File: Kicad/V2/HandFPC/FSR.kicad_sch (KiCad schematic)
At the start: 1 part

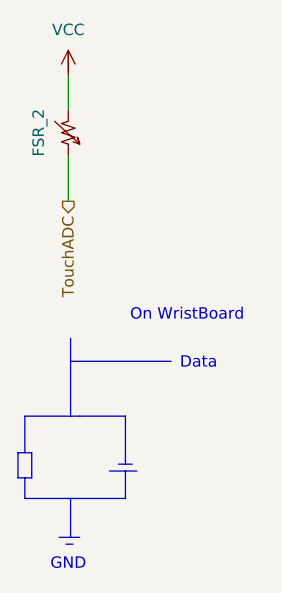
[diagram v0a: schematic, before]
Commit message: hand FPC pass erc no warning no error
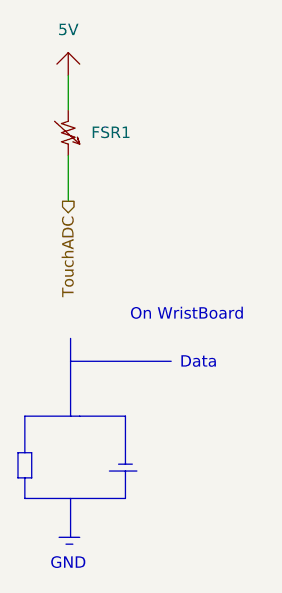
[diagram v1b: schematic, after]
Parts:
- removed FSR_2: (no value), MyGlove:PinHeader_1x02_P2.54mm_Vertical, symbol G-Love:FSR
- added FSR1: (no value), symbol G-Love-Symbols:FSR
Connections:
- net TouchADC: now also FSR1.1
- new net 5V: FSR1.2
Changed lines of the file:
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@@
 	)
 	(symbol
-		(lib_id "G-Love:VCC")
-		(at 33.02 24.13 0)
+		(lib_id "G-Love-Symbols:+5V")
+		(at 33.02 22.86 0)
 		(unit 1)
 		(body_style 1)
@@
 		(dnp no)
 		(fields_autoplaced yes)
-		(property "Reference" "#PWR017"
-			(at 36.83 25.908 0)
+		(property "Reference" "#PWR01"
+			(at 35.56 22.2249 0)
 			(hide yes)
 			(show_name no)
@@
 					(size 1.27 1.27)
 				)
+				(justify left)
 			)
 		)
-		(property "Value" "VCC"
+		(property "Value" "5V"
 			(at 33.02 20.32 0)
 			(show_name no)
@@
 		)
 		(property "Footprint" ""
-			(at 33.02 24.13 0)
+			(at 33.02 22.86 0)
 			(hide yes)
 			(show_name no)
@@
 		)
 		(property "Datasheet" ""
-			(at 33.02 24.13 0)
+			(at 33.02 22.86 0)
 			(hide yes)
 			(show_name no)
@@
 		)
 		(property "Description" ""
-			(at 33.02 24.13 0)
+			(at 33.02 22.86 0)
 			(hide yes)
 			(show_name no)
@@
 			(project "HandFPC"
 				(path "/7221f3d8-f3bc-4a50-a6fd-69c2d8ca27db/03ec02f7-0970-4f94-9fde-cabfa1326b5e"
-					(reference "#PWR017")
+					(reference "#PWR01")
 					(unit 1)
 				)
 				(path "/7221f3d8-f3bc-4a50-a6fd-69c2d8ca27db/15052d3f-5b94-4226-97e2-3e9ab10fafda"
-					(reference "#PWR016")
+					(reference "#PWR02")
 					(unit 1)
 				)
 				(path "/7221f3d8-f3bc-4a50-a6fd-69c2d8ca27db/32c3dc22-6eac-49d0-b512-767615f82205"
-					(reference "#PWR016")
+					(reference "#PWR03")
 					(unit 1)
 				)
 				(path "/7221f3d8-f3bc-4a50-a6fd-69c2d8ca27db/3f48e459-1dc8-4eb9-8adc-befbe01eab22"
-					(reference "#PWR016")
+					(reference "#PWR05")
 					(unit 1)
 				)
 				(path "/7221f3d8-f3bc-4a50-a6fd-69c2d8ca27db/5442b494-eff8-4ddd-bc03-bcc1bea75842"
-					(reference "#PWR016")
+					(reference "#PWR04")
 					(unit 1)
 				)
@@
 	)
 	(symbol
-		(lib_id "G-Love:FSR")
+		(lib_id "G-Love-Symbols:FSR")
 		(at 33.02 31.75 90)
 		(unit 1)
 		(body_style 1)
 		(exclude_from_sim no)
-		(in_bom no)
+		(in_bom yes)
 		(on_board yes)
 		(in_pos_files yes)
 		(dnp no)
-		(property "Reference" "FSR_2"
-			(at 29.718 31.75 0)
+		(fields_autoplaced yes)
+		(property "Reference" "FSR1"
+			(at 35.56 31.7499 90)
 			(show_name no)
 			(do_not_autoplace no)
@@
 					(size 1.27 1.27)
 				)
+				(justify right)
 			)
 		)
@@
 			)
 		)
-		(property "Footprint" "MyGlove:PinHeader_1x02_P2.54mm_Vertical"
+		(property "Footprint" ""
 			(at 33.02 31.75 0)
 			(hide yes)
@@
 			)
 		)
-		(property "Minimum quantity per command" ""
-			(at 33.02 31.75 0)
-			(hide yes)
-			(show_name no)
-			(do_not_autoplace no)
-			(effects
-				(font
-					(size 1.27 1.27)
-				)
-			)
-		)
 		(pin "2"
 		)
@@
 			(project "HandFPC"
 				(path "/7221f3d8-f3bc-4a50-a6fd-69c2d8ca27db/03ec02f7-0970-4f94-9fde-cabfa1326b5e"
-					(reference "FSR_2")
+					(reference "FSR1")
 					(unit 1)
 				)
 				(path "/7221f3d8-f3bc-4a50-a6fd-69c2d8ca27db/15052d3f-5b94-4226-97e2-3e9ab10fafda"
-					(reference "FSR_1")
+					(reference "FSR2")
 					(unit 1)
 				)
 				(path "/7221f3d8-f3bc-4a50-a6fd-69c2d8ca27db/32c3dc22-6eac-49d0-b512-767615f82205"
-					(reference "FSR_1")
+					(reference "FSR3")
 					(unit 1)
 				)
 				(path "/7221f3d8-f3bc-4a50-a6fd-69c2d8ca27db/3f48e459-1dc8-4eb9-8adc-befbe01eab22"
-					(reference "FSR_1")
+					(reference "FSR5")
 					(unit 1)
 				)
 				(path "/7221f3d8-f3bc-4a50-a6fd-69c2d8ca27db/5442b494-eff8-4ddd-bc03-bcc1bea75842"
-					(reference "FSR_1")
+					(reference "FSR4")
 					(unit 1)
 				)

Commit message: add FPC footprints
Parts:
- FSR1: footprint (none) -> MyGlove:FPC_FSR
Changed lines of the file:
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@@
 			)
 		)
-		(property "Footprint" ""
+		(property "Footprint" "MyGlove:FPC_FSR"
 			(at 33.02 31.75 0)
 			(hide yes)

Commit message: add routing
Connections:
- net 5V renamed +3.3V
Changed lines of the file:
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@@
 	)
 	(symbol
-		(lib_id "G-Love-Symbols:+5V")
-		(at 33.02 22.86 0)
+		(lib_id "G-Love-Symbols:+3.3V")
+		(at 33.02 24.13 0)
 		(unit 1)
 		(body_style 1)
@@
 		(in_pos_files yes)
 		(dnp no)
-		(fields_autoplaced yes)
 		(property "Reference" "#PWR012"
-			(at 35.56 22.2249 0)
+			(at 36.83 25.908 0)
 			(hide yes)
 			(show_name no)
@@
 					(size 1.27 1.27)
 				)
-				(justify left)
 			)
 		)
-		(property "Value" "5V"
-			(at 33.02 20.32 0)
+		(property "Value" "+3.3V"
+			(at 36.322 22.606 0)
 			(show_name no)
 			(do_not_autoplace no)
@@
 		)
 		(property "Footprint" ""
-			(at 33.02 22.86 0)
+			(at 33.02 24.13 0)
 			(hide yes)
 			(show_name no)
@@
 		)
 		(property "Datasheet" ""
-			(at 33.02 22.86 0)
+			(at 33.02 24.13 0)
 			(hide yes)
 			(show_name no)
@@
 		)
 		(property "Description" ""
-			(at 33.02 22.86 0)
+			(at 33.02 24.13 0)
 			(hide yes)
 			(show_name no)
@@
 				)
 				(path "/7221f3d8-f3bc-4a50-a6fd-69c2d8ca27db/15052d3f-5b94-4226-97e2-3e9ab10fafda"
+					(reference "#PWR018")
+					(unit 1)
+				)
+				(path "/7221f3d8-f3bc-4a50-a6fd-69c2d8ca27db/32c3dc22-6eac-49d0-b512-767615f82205"
+					(reference "#PWR019")
+					(unit 1)
+				)
+				(path "/7221f3d8-f3bc-4a50-a6fd-69c2d8ca27db/3f48e459-1dc8-4eb9-8adc-befbe01eab22"
+					(reference "#PWR021")
+					(unit 1)
+				)
+				(path "/7221f3d8-f3bc-4a50-a6fd-69c2d8ca27db/5442b494-eff8-4ddd-bc03-bcc1bea75842"
 					(reference "#PWR020")
 					(unit 1)
 				)
-				(path "/7221f3d8-f3bc-4a50-a6fd-69c2d8ca27db/32c3dc22-6eac-49d0-b512-767615f82205"
-					(reference "#PWR021")
-					(unit 1)
-				)
-				(path "/7221f3d8-f3bc-4a50-a6fd-69c2d8ca27db/3f48e459-1dc8-4eb9-8adc-befbe01eab22"
-					(reference "#PWR023")
-					(unit 1)
-				)
-				(path "/7221f3d8-f3bc-4a50-a6fd-69c2d8ca27db/5442b494-eff8-4ddd-bc03-bcc1bea75842"
-					(reference "#PWR022")
-					(unit 1)
-				)
